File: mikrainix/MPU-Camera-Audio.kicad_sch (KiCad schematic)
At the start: 8 parts, among them J3 Conn_01x20_Pin, U7 RV1106G3

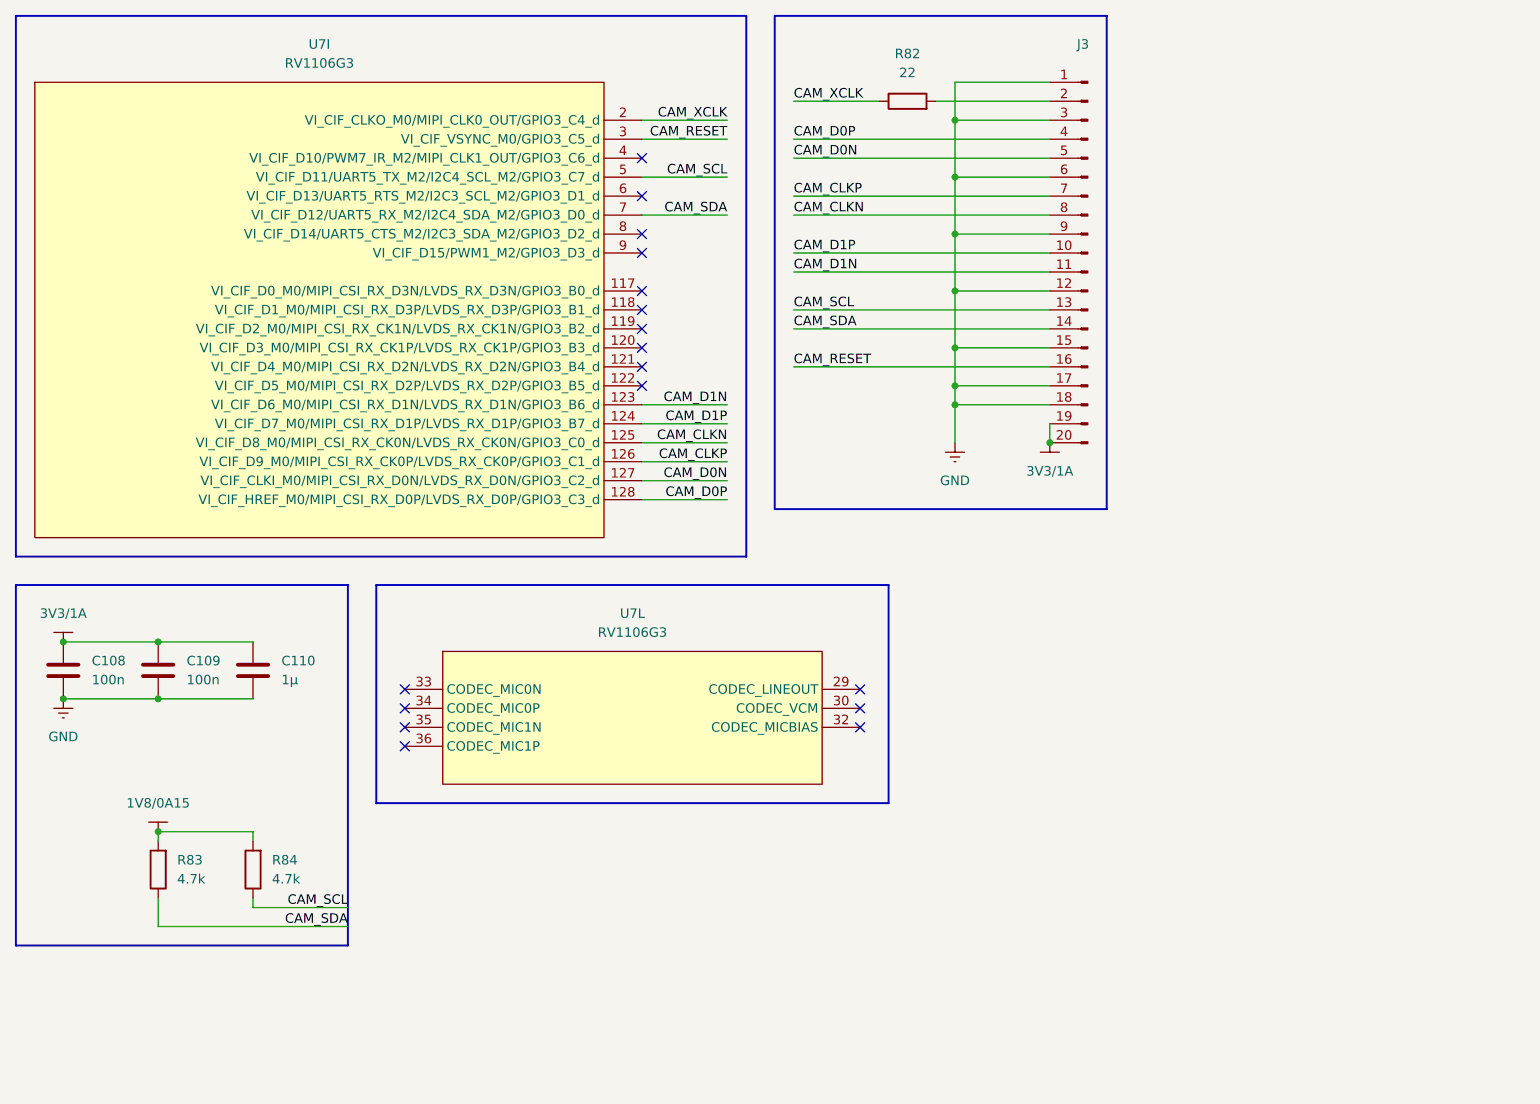
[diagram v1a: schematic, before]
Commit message: add ESD protection
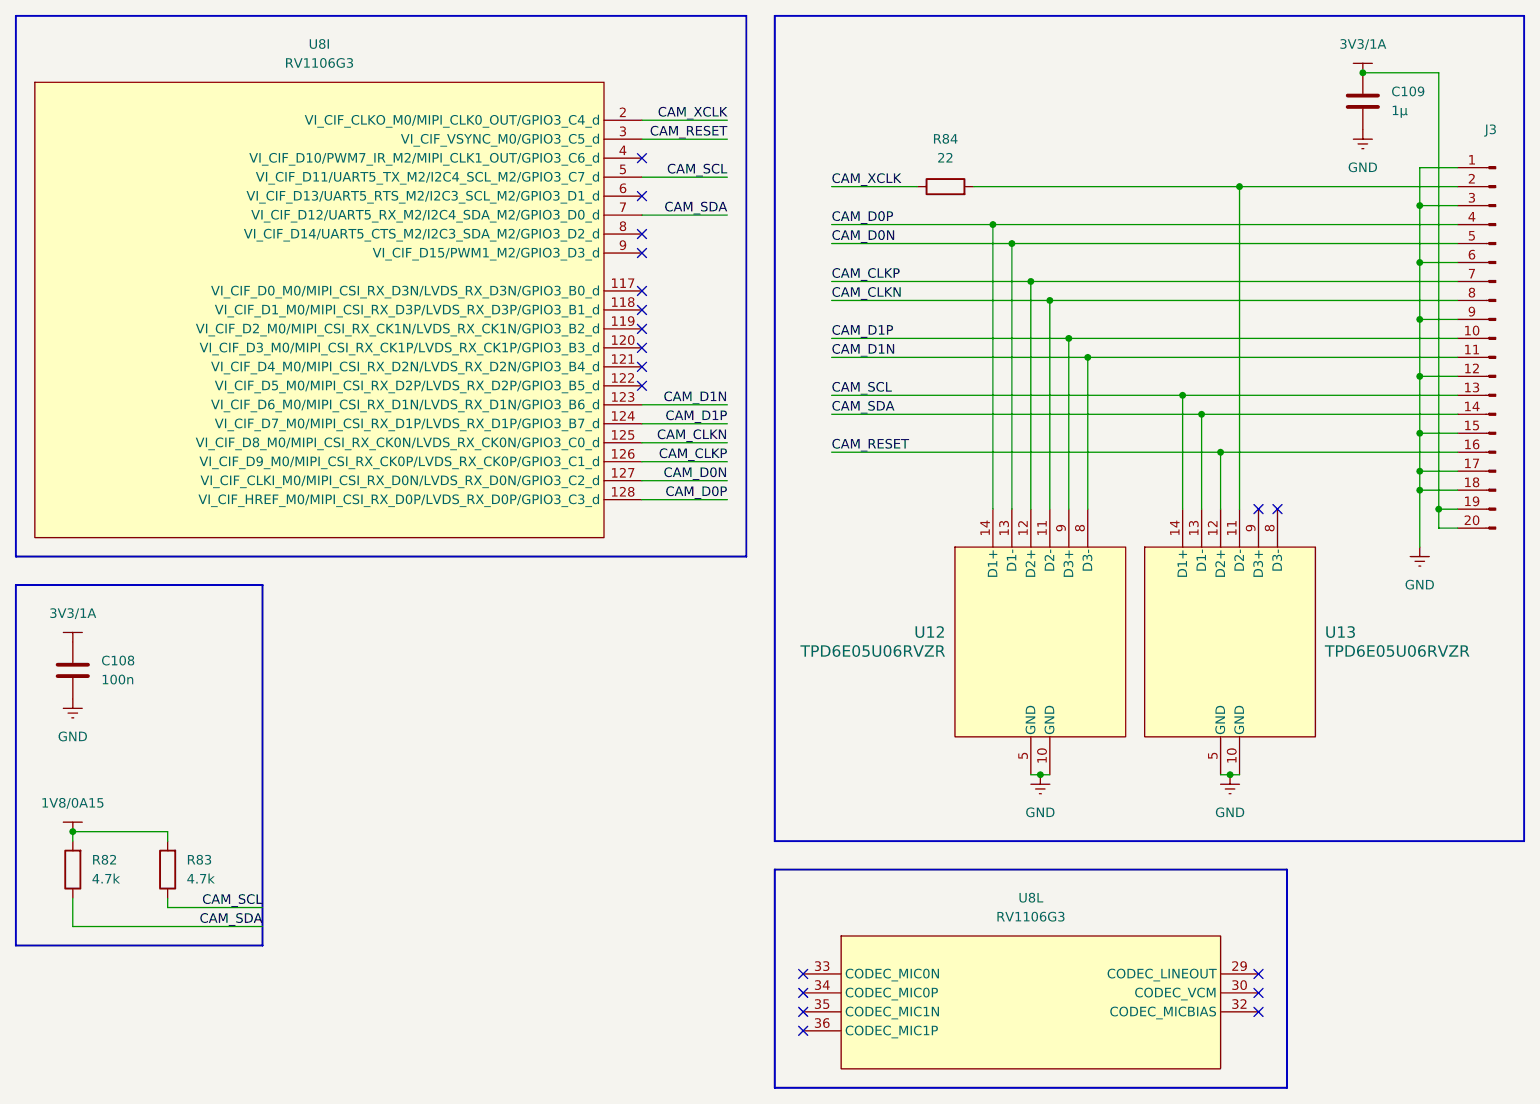
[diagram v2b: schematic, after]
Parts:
- removed C110: 1µ, symbol Device:C
- removed U7: RV1106G3, mikrainix-RV1106G3:QFN35P1230X1230X90-129N, symbol mikrainix-RV1106G3:RV1106G3
- added U12, U13: TPD6E05U06RVZR, mikrainix-TPD6E05U06RVZR:RVZ0014A, symbol mikrainix-TPD6E05U06RVZR:TPD6E05U06RVZR
- added U8: RV1106G3, mikrainix-RV1106G3:QFN35P1230X1230X90-129N, symbol mikrainix-RV1106G3:RV1106G3
- C109: value 100n -> 1µ
- renumbered R83 to R82, R84 to R83, R82 to R84
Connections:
- net CAM_CLKN: now also U12.11 (D2-), U8.125 (VI_CIF_D8_M0/MIPI_CSI_RX_CK0N/LVDS_RX_CK0N/GPIO3_C0_d)
- net CAM_CLKP: now also U12.12 (D2+), U8.126 (VI_CIF_D9_M0/MIPI_CSI_RX_CK0P/LVDS_RX_CK0P/GPIO3_C1_d)
- net CAM_D0N: now also U12.13 (D1-), U8.127 (VI_CIF_CLKI_M0/MIPI_CSI_RX_D0N/LVDS_RX_D0N/GPIO3_C2_d)
- net CAM_D0P: now also U12.14 (D1+), U8.128 (VI_CIF_HREF_M0/MIPI_CSI_RX_D0P/LVDS_RX_D0P/GPIO3_C3_d)
- net CAM_D1N: now also U12.8 (D3-), U8.123 (VI_CIF_D6_M0/MIPI_CSI_RX_D1N/LVDS_RX_D1N/GPIO3_B6_d)
- net CAM_D1P: now also U12.9 (D3+), U8.124 (VI_CIF_D7_M0/MIPI_CSI_RX_D1P/LVDS_RX_D1P/GPIO3_B7_d)
- net CAM_RESET: now also U12.4 (NC), U13.12 (D2+), U8.3 (VI_CIF_VSYNC_M0/GPIO3_C5_d)
- net CAM_SCL: now also U12.2 (NC), U13.14 (D1+), U8.5 (VI_CIF_D11/UART5_TX_M2/I2C4_SCL_M2/GPIO3_C7_d)
- net CAM_SDA: now also U12.3 (NC), U13.13 (D1-), U8.7 (VI_CIF_D12/UART5_RX_M2/I2C4_SDA_M2/GPIO3_D0_d)
- net CAM_XCLK: now also U8.2 (VI_CIF_CLKO_M0/MIPI_CLK0_OUT/GPIO3_C4_d)
- net GND: now also U12.10 (GND), U12.5 (GND), U13.10 (GND), U13.5 (GND)
- net at J3.2 (Pin_2), R84.2: now also U12.6 (NC), U13.11 (D2-)
- new net: U12.7 (NC), U13.9 (D3+)
- no-connect marks 17 -> 19
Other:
- moved on the sheet: C108, J3, R82, R83, R84
